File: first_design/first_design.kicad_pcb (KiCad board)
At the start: 2 copper layers, 157 x 57 mm, 55 parts, among them J1 Conn_02x20_Odd_Even, J2 Accelerometer_small, J3 Accelerometer_standard, J4 Servo_motor, SW1 SW_DPST, SW2 SW_DPST, SW3 SW_DPST, SW4 SW_DPST

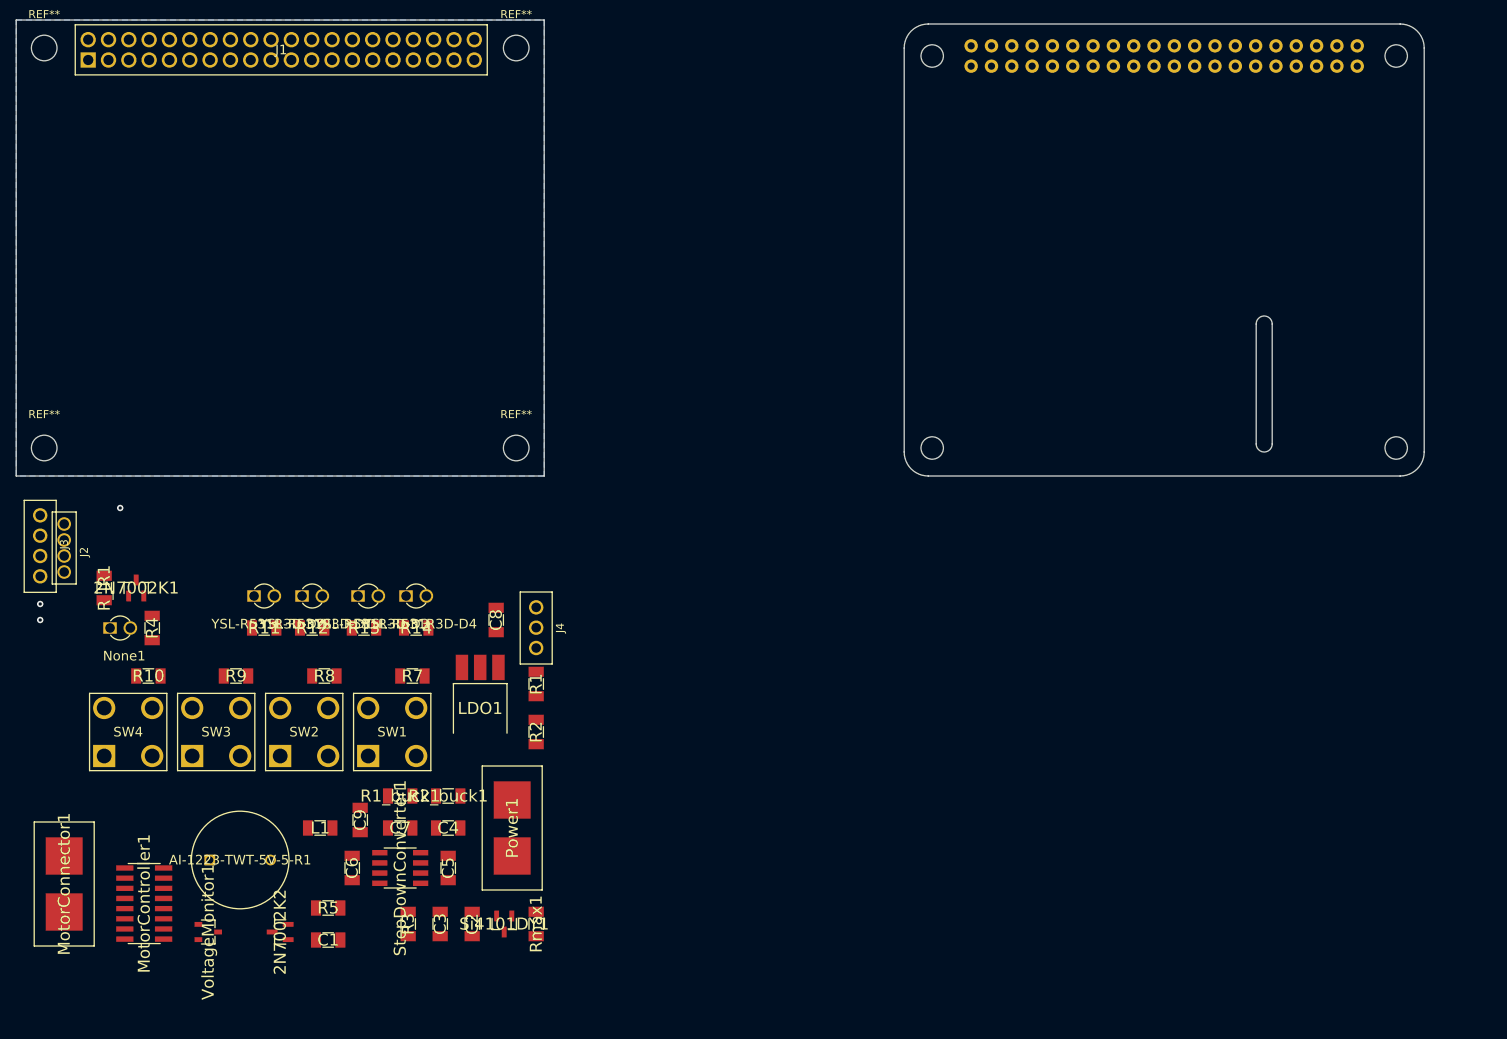
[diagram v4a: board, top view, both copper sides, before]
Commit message: fitting components in piHat
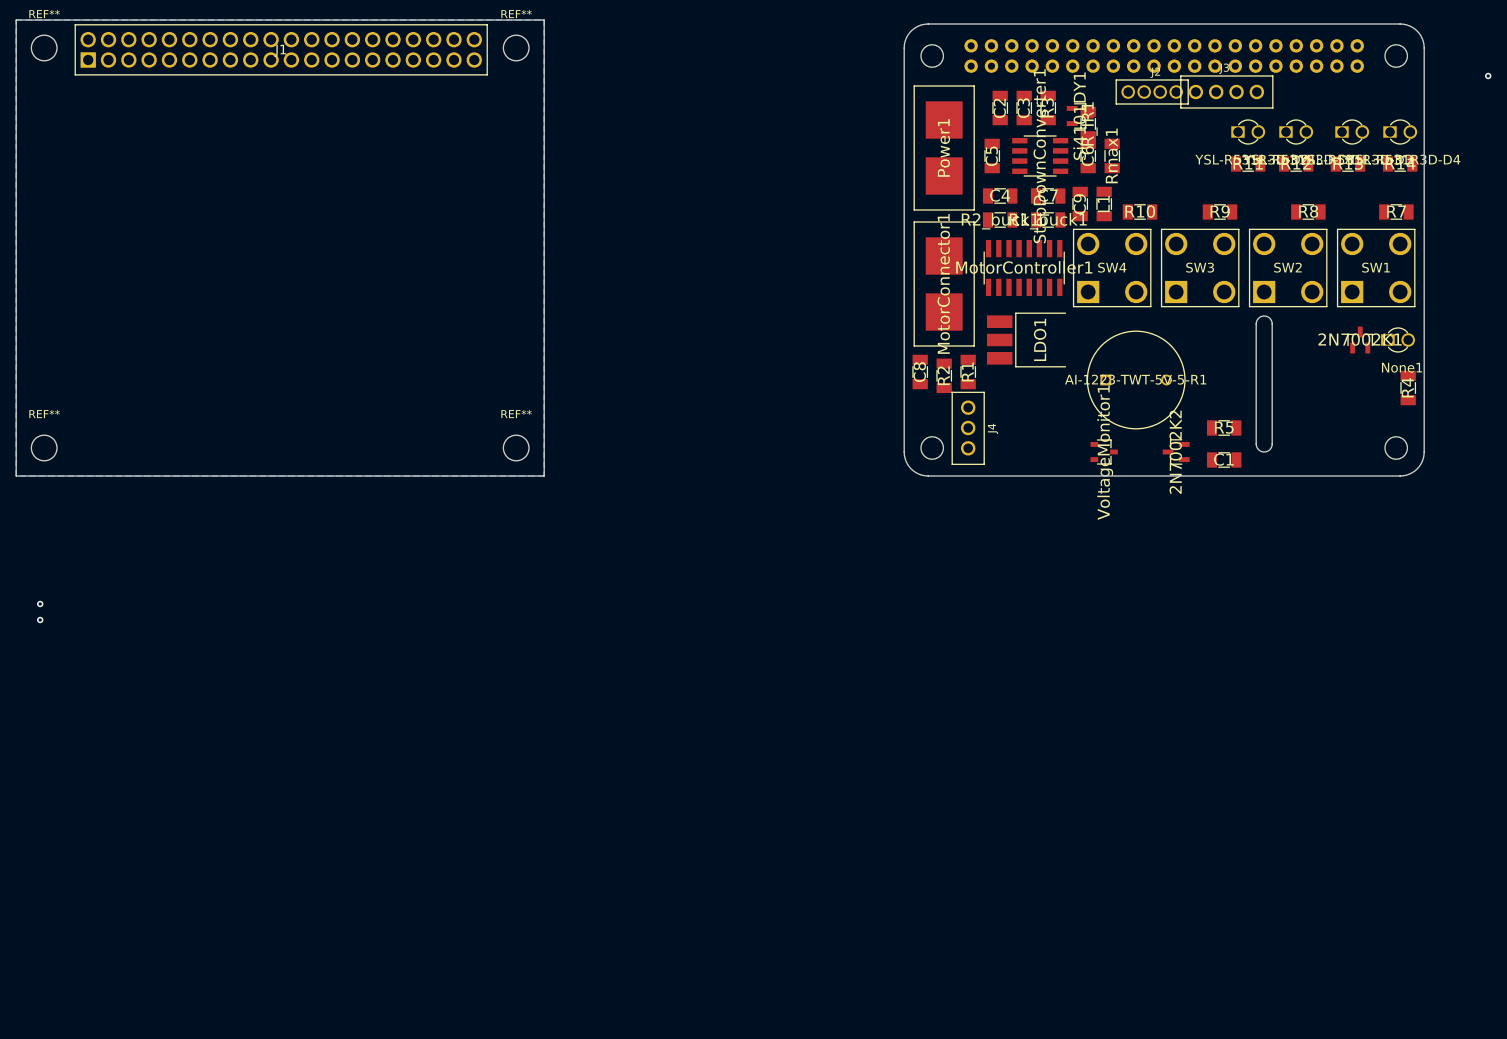
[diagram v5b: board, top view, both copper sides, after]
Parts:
- moved None1 163.7 mm to (196.7, 64.0)
- moved J3 163.7 mm to (179.1, 33.0), turned to 180 degrees
- moved R4 159.8 mm to (198.0, 70.0)
- moved 2N7002K1 156.1 mm to (192.0, 64.0)
- moved J2 151.4 mm to (169.0, 33.0), turned to 180 degrees
- moved R10 136.8 mm to (164.5, 48.0)
- moved R11 136.0 mm to (178.0, 42.0)
- moved R12 136.0 mm to (184.0, 42.0)
- moved R13 136.0 mm to (190.5, 42.0)
- moved R14 136.0 mm to (197.0, 42.0)
- moved R7 136.0 mm to (196.5, 48.0)
- moved R8 136.0 mm to (185.5, 48.0)
- moved R9 136.0 mm to (174.5, 48.0)
- moved R_IR1 136.0 mm to (158.0, 37.0)
- moved SW1 136.0 mm to (191.0, 58.0)
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
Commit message: Night Session
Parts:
- removed the REF** at (27.5, 77.5)
- removed the REF** at (27.5, 27.5)
- removed the REF** at (86.5, 77.5)
- added REF**: MountingHole_2.7mm_M2.5, MountingHole:MountingHole_2.7mm_M2.5, F.Cu at (3.50, -3.50)
- added REF**: MountingHole_2.7mm_M2.5, MountingHole:MountingHole_2.7mm_M2.5, F.Cu at (3.50, -52.5)
- added REF**: MountingHole_2.7mm_M2.5, MountingHole:MountingHole_2.7mm_M2.5, F.Cu at (61.5, -3.50)
- REF**: value MountingHole_3.2mm_M3 -> MountingHole_2.7mm_M2.5; footprint MountingHole:MountingHole_3.2mm_M3 -> MountingHole:MountingHole_2.7mm_M2.5
- moved C4 184.5 mm to (-17.0, -38.5)
- moved C7 184.5 mm to (-11.0, -38.5)
- moved R1_buck1 184.5 mm to (-11.0, -35.5)
- moved R2_buck1 184.5 mm to (-17.0, -35.5)
- moved StepDownConverter1 177.1 mm to (-12.5, -24.5)
- moved C6 170.1 mm to (11.5, -45.5)
- moved MotorController1 168.5 mm to (9.50, -38.0), turned to 90 degrees
- moved MotorConnector1 165.9 mm to (3.00, -36.5)
- moved VoltageMonitor1 164.5 mm to (16.5, -2.50)
- moved Rmax1 161.8 mm to (12.0, -22.0), turned to 0 degrees
- moved Si4101DY1 160.0 mm to (9.50, -26.0), turned to 90 degrees
- moved 2N7002K1 157.8 mm to (56.0, -16.0)
- moved 2N7002K2 157.8 mm to (33.0, -2.00)
- moved AI-1223-TWT-5V-5-R1 157.8 mm to (28.0, -11.0)
- moved C1 157.8 mm to (39.0, -1.00)
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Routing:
- net Net-(C7-Pad1): track 0.00 -> 17.9 mm
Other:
- board size 157 x 57 mm -> 65 x 56.5 mm

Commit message: board
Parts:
- removed REF** (x4): MountingHole_2.7mm_M2.5, MountingHole:MountingHole_2.7mm_M2.5
- removed RPI1: RASPBERRYPI_BPLUS_HATNOSLOTS, Adafruit HaD Proto HAT rev A:PI_HAT_NOSLOTS
- removed SW1, SW2, SW3, SW4: SW_DPST, library_express_pro:button_6x6mm
- added H1: MountingHole, MountingHole:MountingHole_2.7mm_M2.5, F.Cu at (3.50, -52.5)
- added H2: MountingHole, MountingHole:MountingHole_2.7mm_M2.5, F.Cu at (61.5, -52.5)
- added H3: MountingHole, MountingHole:MountingHole_2.7mm_M2.5, F.Cu at (3.50, -3.50)
- added H4: MountingHole, MountingHole:MountingHole_2.7mm_M2.5, F.Cu at (61.5, -3.50)
- added JP1: Jumper, library_express_pro:standard_jumper, F.Cu at (27.0, -12.5)
- added PTS636_G_Leads1: led3, library_express_pro:PTS636, F.Cu at (47.5, -26.0)
- added PTS636_G_Leads2: led2, library_express_pro:PTS636, F.Cu at (54.5, -26.0)
- added PTS636_G_Leads3: led4, library_express_pro:PTS636, F.Cu at (40.5, -26.0)
- added PTS636_G_Leads4: led1, library_express_pro:PTS636, F.Cu at (61.5, -26.0)
- AI1027TWT5V2R1: renamed from AI-1223-TWT-5V-5-R1; footprint library_express_pro:Buzzer_AI-1223-TWT-5V-5-R -> library_express_pro:Buzzer_AI1027TWT5V2R
- SQJA37EP1: renamed from Si4101DY1; footprint library_express_pro:SOT23 -> library_express_pro:SO-8L
- moved J4 34.8 mm to (5.00, -8.00), turned to 0 degrees
- moved R1_buck1 33.5 mm to (22.5, -37.0)
- moved StepDownConverter1 29.9 mm to (16.0, -33.5), turned to 180 degrees
- moved C4 28.4 mm to (11.0, -34.0), turned to 90 degrees
- moved R2_buck1 24.5 mm to (7.50, -34.0), turned to 90 degrees
- moved VoltageMonitor1 22.3 mm to (22.5, -24.0)
- moved C1 21.9 mm to (23.5, -16.5)
- moved R5 21.6 mm to (23.5, -20.0)
- moved C6 18.2 mm to (22.5, -31.0), turned to 0 degrees
- moved C7 16.1 mm to (3.00, -46.5)
- moved 2N7002K2 14.8 mm to (22.5, -12.5)
- moved C3 12.9 mm to (21.0, -27.5), turned to 0 degrees
- moved LDO1 12.5 mm to (16.5, -19.5), turned to 180 degrees
- moved AI1027TWT5V2R1 12.3 mm to (16.5, -6.50)
- moved R10 10.2 mm to (40.5, -34.0)
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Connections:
- SQJA37EP1 pad 1: +7.5V -> Vbat
- SQJA37EP1 pad 3: Net-(D1-Pad2) -> Vbat
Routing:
- net Net-(C7-Pad1): track 17.9 -> 0.00 mm

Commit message: tracing
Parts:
- removed C7: 44uF, library_express_pro:RLC_EIA_3216
- removed R3: 100K, library_express_pro:RLC_EIA_3216
- C2: value 170uF -> 10uF
- YSL-R531R3D-D1, YSL-R531R3D-D2, YSL-R531R3D-D3, YSL-R531R3D-D4: footprint library_express_pro:LED_YSL-R531R3D-D2 -> library_express_pro:RLC_EIA_3216
- moved AI1027TWT5V2R1 61.5 mm to (78.0, -6.00)
- moved J3 50.6 mm to (-6.50, -47.0), turned to 270 degrees
- moved J2 38.0 mm to (-4.00, -46.5), turned to 270 degrees
- moved C1 34.3 mm to (55.0, -30.0)
- moved YSL-R531R3D-D4 33.2 mm to (58.0, -9.50), turned to 90 degrees
- moved VoltageMonitor1 33.0 mm to (54.0, -34.0), turned to 90 degrees
- moved R5 31.4 mm to (54.5, -25.0)
- moved R14 30.1 mm to (91.5, -41.0)
- moved R7 30.1 mm to (91.5, -37.0)
- moved R11 30.1 mm to (70.5, -40.5)
- moved R12 30.1 mm to (77.5, -40.5)
- moved R13 30.1 mm to (84.5, -40.5)
- moved R10 30.1 mm to (70.5, -36.5)
- moved R8 30.1 mm to (84.5, -36.5)
- moved R9 30.1 mm to (77.5, -36.5)
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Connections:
- J4 pad 1: 6V-5V -> GND
- J4 pad 2: GND -> 6V-5V
- Rmax1 pad 1: Net-(D1-Pad2) -> Net-(Rmax1-Pad1)
- SQJA37EP1 pad 1: Vbat -> +7.5V
- SQJA37EP1 pad 3: Vbat -> Net-(Rmax1-Pad1)
- StepDownConverter1 pad 1: Net-(R3-Pad1) -> Vbat
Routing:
- net Net-(Rmax1-Pad1): track 0.00 -> 22.2 mm, vias 0 -> 2
- net GND: track 0.00 -> 10.9 mm, vias 3 -> 25
- net motor_PWM: track 0.00 -> 7.60 mm, vias 0 -> 1
- net Net-(LDO1-Pad1): track 0.00 -> 7.20 mm
- net Vbat: track 0.00 -> 4.85 mm, vias 0 -> 20
- net 6V-5V: track 0.00 -> 4.42 mm
- net motor_INB: track 0.00 -> 2.40 mm
- net motor_INA: track 0.00 -> 1.34 mm
- added copper zone on F.Cu, net +7.5V
- added copper zone on F.Cu, net 6V-5V
- added copper zone on F.Cu, net GND
- added copper zone on F.Cu, net Net-(MotorConnector1-Pad1)
- added copper zone on F.Cu, net Net-(MotorConnector1-Pad2)
- added copper zone on B.Cu, net Vbat
- added copper zone on F.Cu, net Vbat
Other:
- rule pad_to_mask_clearance: 0.051 -> 0.1
- rule trace_min: 0.2 -> 0.15
- rule via_min_size: 0.4 -> 0.3
